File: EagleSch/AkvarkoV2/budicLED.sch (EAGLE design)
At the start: 66 parts, among them IC1 7805T, IC2 4051N, IC3 LF33CV, IC4 ESP01, Q1 BD243C, Q2 BD243C, Q3 BD243C, Q4 BD243C, T1 2N5551, T2 2N5551, T3 2N5551, T4 2N5551, U1 ARDUINOR3-DIMENSION, X1 SMKDSP_1,5/2, X2 SMKDSP_1,5/8, X3 SMKDSP_1,5/3

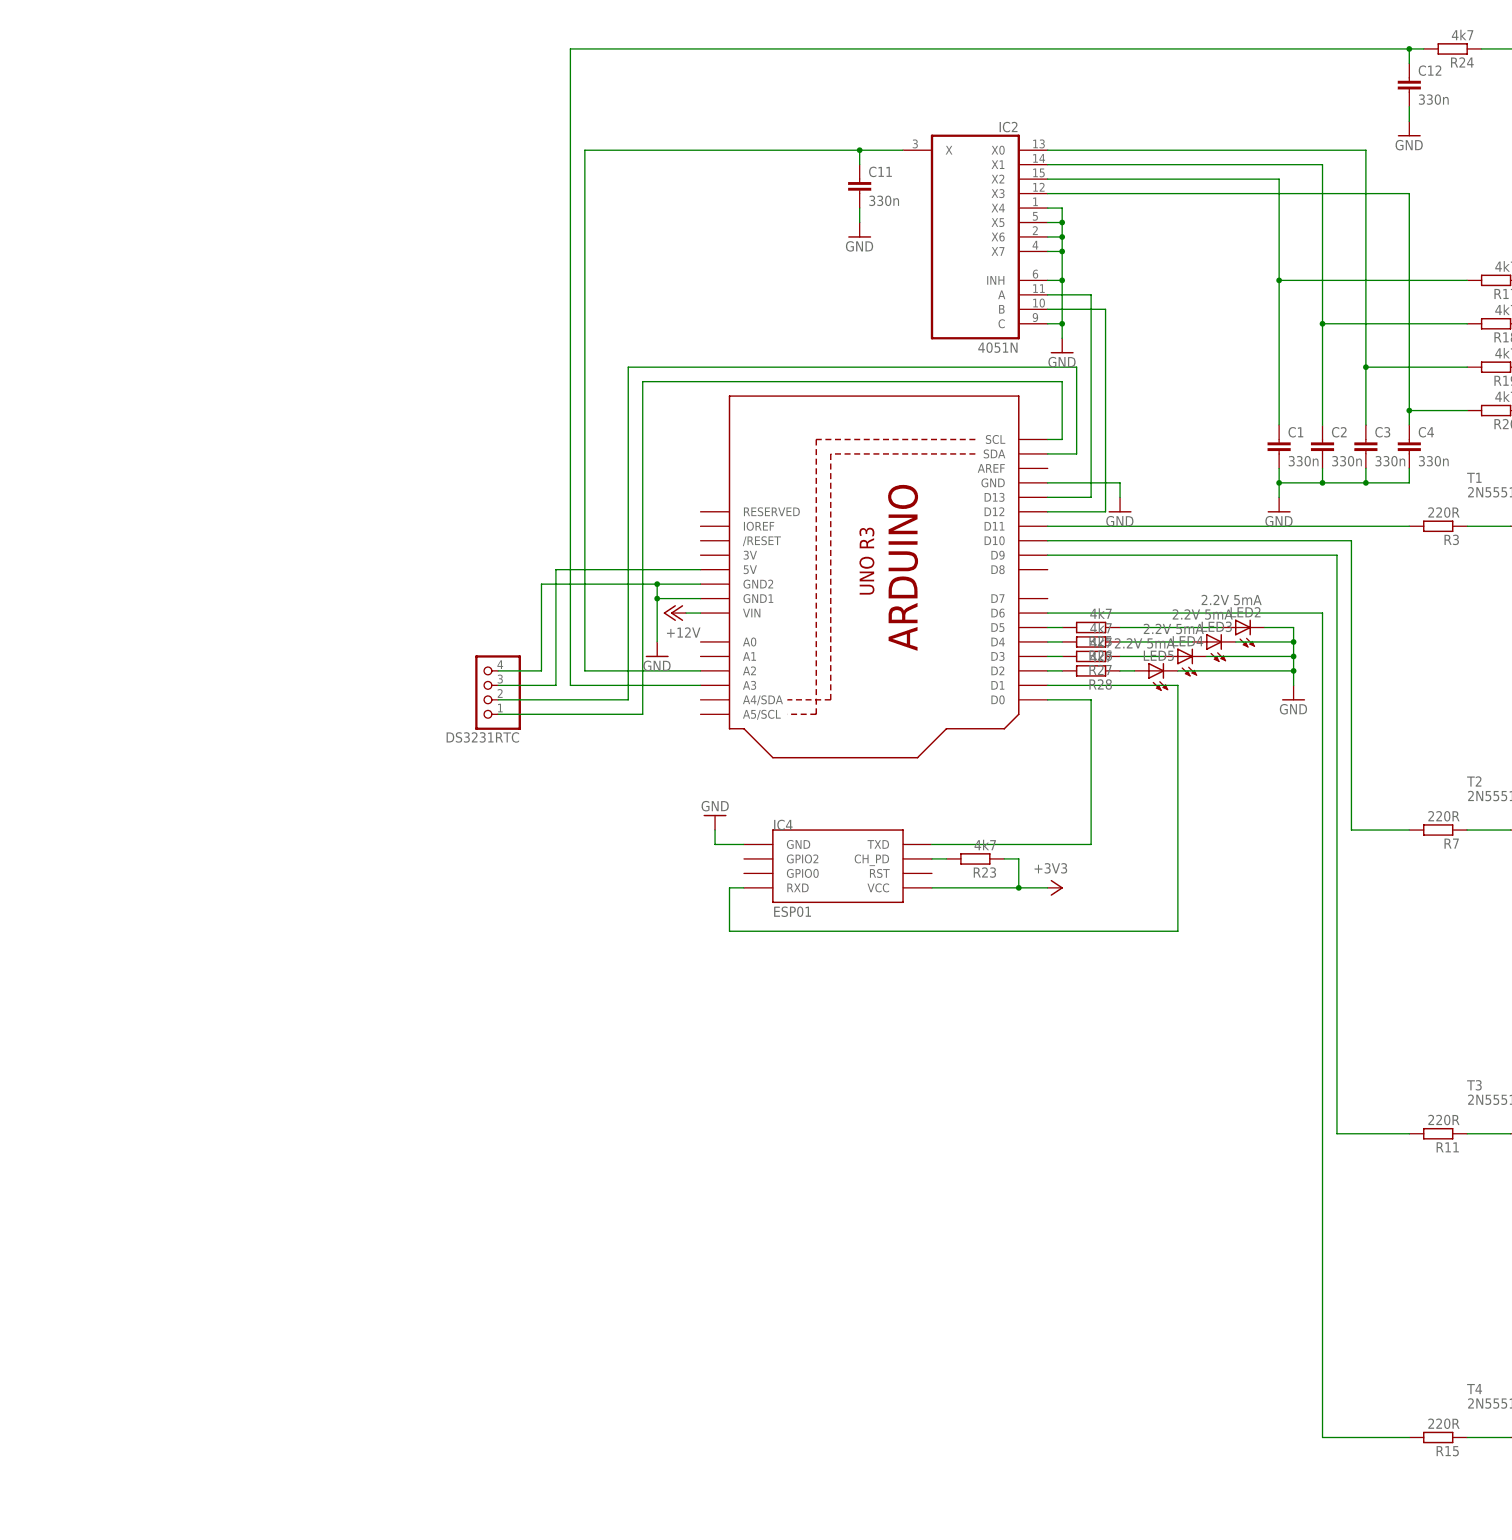
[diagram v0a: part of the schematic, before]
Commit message: Pridan slot pro SD kartu, odstraneny signalizacni diody.
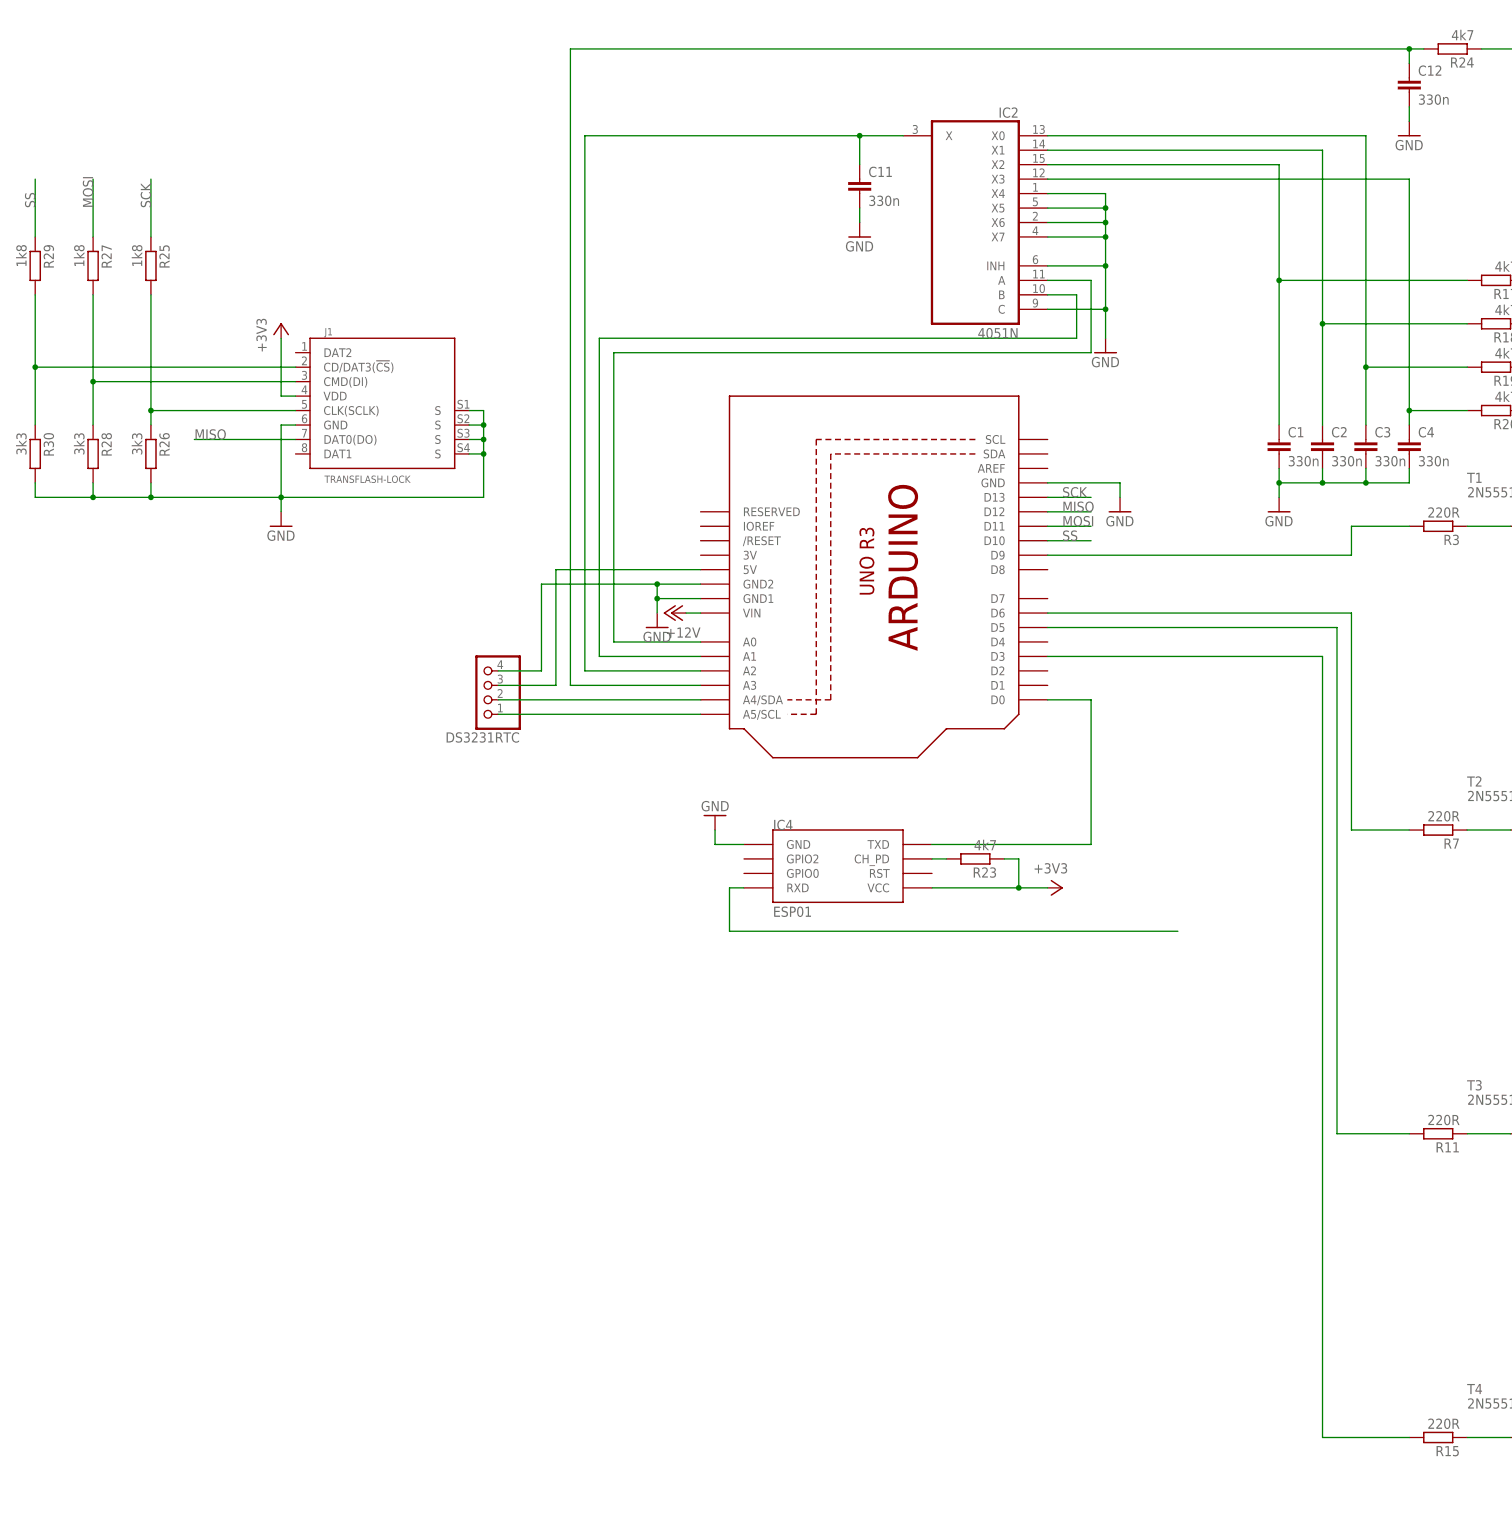
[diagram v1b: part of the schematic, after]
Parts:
- removed LED2, LED3, LED4, LED5: 2.2V 5mA, led:LED3MM
- added J1: TRANSFLASH-LOCK, sd-mmc:TRANSFLASH-LOCK
- added R29: 1k8, rcl:R-EU_R0805
- added R30: 3k3, rcl:R-EU_R0805
- R25, R27: value 4k7 -> 1k8
- R26, R28: value 4k7 -> 3k3
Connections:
- removed net N$20: IC2A.A, U1.D13
- removed net N$38: LED5.A, R28.1
- removed net N$39: LED4.A, R27.1
- removed net N$40: LED3.A, R26.1
- removed net N$41: LED2.A, R25.1
- new net MISO: J1.DAT0(DO), U1.D12
- new net MOSI: R27.1, U1.D11
- new net SCK: R25.1, U1.D13
- new net SS: R29.1, U1.D10
- net +3V3: now also J1.VDD
- net GND: now also J1.GND, J1.S@1, J1.S@2, J1.S@3, J1.S@4, R26.2, R28.2, R30.2; no longer LED2.C, LED3.C, LED4.C, LED5.C
- net N$13: now also U1.A5/SCL; no longer U1.SCL
- net N$15: now also U1.D5; no longer U1.D9
- net N$16: now also R3.2, U1.D9; no longer R28.2, U1.D2
- net N$22: now also U1.D6; no longer U1.D10
- net N$24: now also U1.A4/SDA; no longer U1.SDA
- net N$26: now also IC2A.A, U1.A0; no longer R27.2, U1.D3
- net N$28: no longer U1.D1
- net N$32: now also J1.CLK(SCLK), R25.2, R26.1; no longer IC2A.B, U1.D12
- net N$34: now also IC2A.B, U1.A1; no longer R3.2, U1.D11
- net N$35: now also U1.D3; no longer U1.D6
- net N$36: now also J1.CMD(DI), R27.2, R28.1; no longer R26.2, U1.D4
- net N$37: now also J1.CD/DAT3(!CS!), R29.2, R30.1; no longer R25.2, U1.D5
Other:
- moved on the sheet: IC2, R25, R26, R27, R28

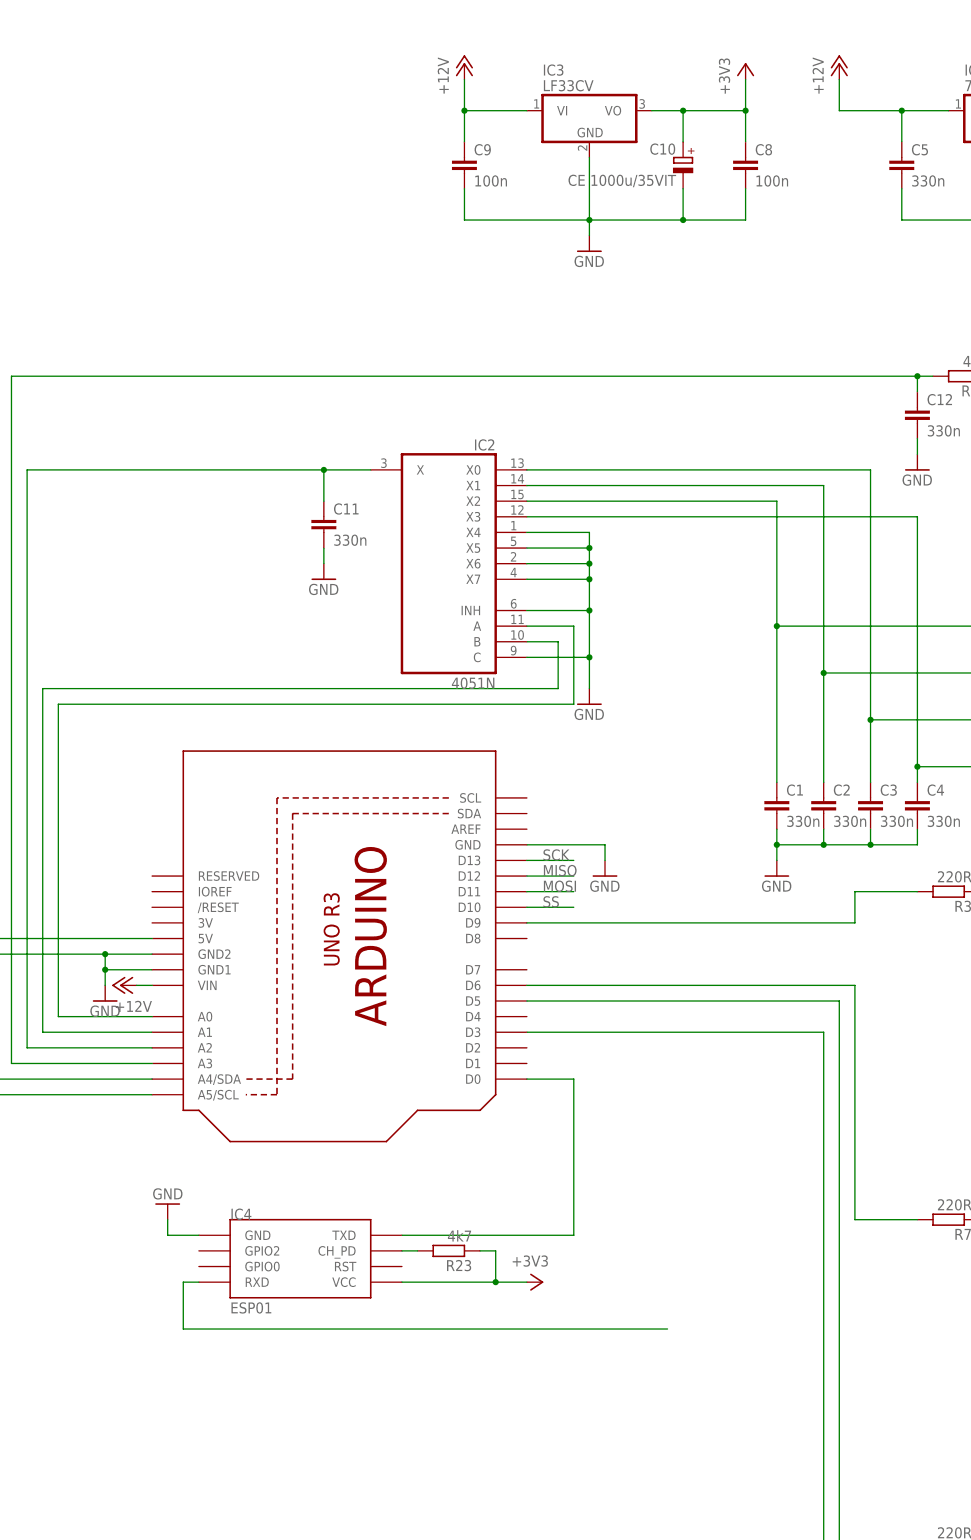
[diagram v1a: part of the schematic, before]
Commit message: Na DPS: - upraveno napajeni - zmenena pouzdra rezistoru u SD karty - seriova linka vyvedena na kolikovou listu - zvetsena sirka spoje GND, doplnen jeden filtracni kapacitor k SD slotu
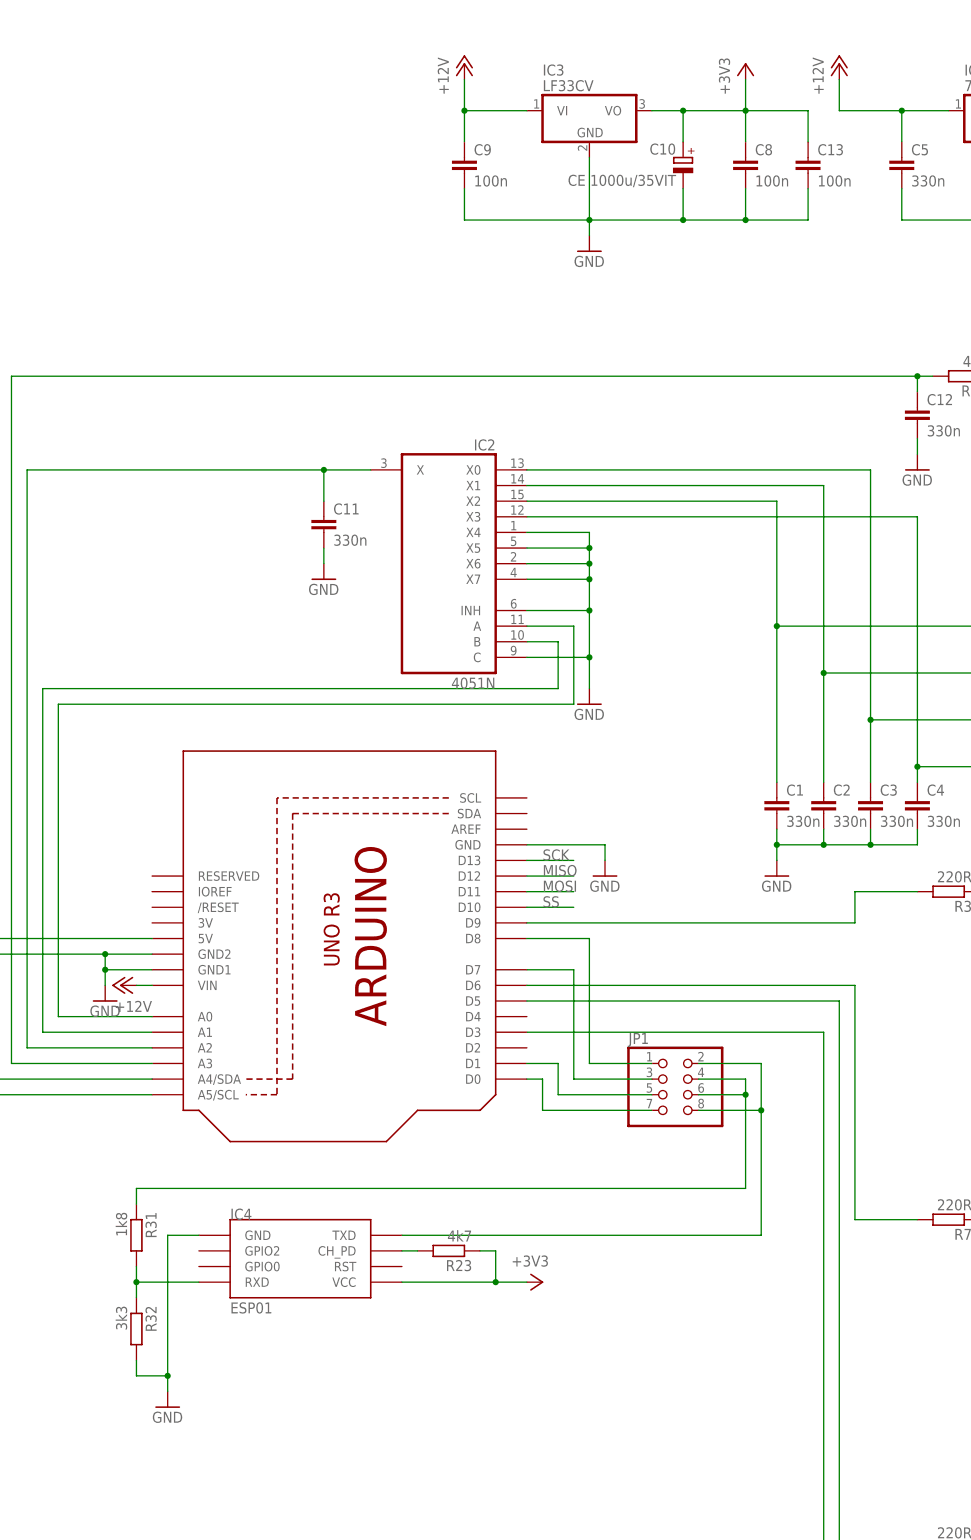
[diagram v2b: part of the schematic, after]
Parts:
- added C13: 100n, rcl:C-EUC1206K
- added JP1: (no value), pinhead:PINHD-2X4
- added R31: 1k8, rcl:R-EU_0207/12
- added R32: 3k3, rcl:R-EU_0207/12
- R25, R26, R27, R28, R29, R30: device rcl:R-EU_R0805 -> rcl:R-EU_0207/12
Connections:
- new net N$20: IC4.TXD, JP1.2, JP1.8
- new net N$38: JP1.5, U1.D1
- new net N$39: IC4.RXD, R31.2, R32.1
- new net N$41: JP1.7, U1.D0
- new net N$42: JP1.1, U1.D8
- net +3V3: now also C13.1
- net GND: now also C13.2, R32.2
- net N$25: now also JP1.4, JP1.6, R31.1; no longer IC4.TXD, U1.D0
- net N$28: now also JP1.3, U1.D7; no longer IC4.RXD

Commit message: DPS: - pridany LED, - dratove propojky nahrazeny reszistory 0R0, - doplnena rozlita med, - pridan zesilovaci prvek (tranzistor) k AD prevodnikum od snimani proudu ve vykonovem obvodu, - pridano nekolik filtracnich kapacit u napajeni IO.
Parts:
- added C14, C15: 330n, rcl:C-EUC1206K
- added LED2, LED3: 2.2V 25mA, led:LED3MM
- added Q5: BC546A, transistor-npn:BC546A
- added R33, R34, R35: 10k, rcl:R-EU_0207/12
- added R36, R37: 390R, rcl:R-EU_0207/12
- added R38: 0R0, rcl:R-EU_0207/15
- added R39, R40, R41: 0R0, rcl:R-EU_0207/12
- C11: device rcl:C-EUC0805K -> rcl:C-EUC1206K
- R17, R18, R19, R20: value 4k7 -> 1k
- R24: device rcl:R-EU_R0805 -> rcl:R-EU_0207/15
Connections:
- new net GNDA: C1.2, C11.2, C12.2, C15.2, C2.2, C3.2, C4.2, IC2A.C, IC2A.INH, IC2A.X4, IC2A.X5, IC2A.X6, IC2A.X7, IC2P.GND, IC2P.VEE, R39.1
- new net LEDA: LED2.A, U1.D4
- new net LEDB: LED3.A, U1.D2
- new net N$40: C11.1, IC2A.X, Q5.E
- new net N$43: LED2.C, R36.2
- new net N$44: DS3231RTC.3, R33.2, R34.1, U1.5V
- new net N$45: LED3.C, R37.2
- new net N$46: C15.1, IC2P.VCC, R38.1
- new net N$47: J1.VDD, R40.2
- new net N$49: C13.1, R40.1, R41.1
- net +3V3: now also R41.2; no longer C13.1, J1.VDD
- net GND: now also R35.2, R36.1, R37.1, R39.2; no longer C1.2, C11.2, C12.2, C2.2, C3.2, C4.2, IC2A.C, IC2A.INH, IC2A.X4, IC2A.X5, IC2A.X6, IC2A.X7, IC2P.GND, IC2P.VEE
- net N$18: now also C14.1, Q5.C, R33.1; no longer C11.1, IC2A.X
- net N$19: now also C14.2, Q5.B, R34.2, R35.1; no longer DS3231RTC.3, U1.5V
- net N$23: now also R38.2; no longer IC2P.VCC
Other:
- moved on the sheet: C13, IC2P
